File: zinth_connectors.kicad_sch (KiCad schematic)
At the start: 20 parts, among them J3 qwiic, J4 HeaderMale-2.54_1x16, J5 usb, J6 qwiic, J8 HeaderMale-2.54_1x16

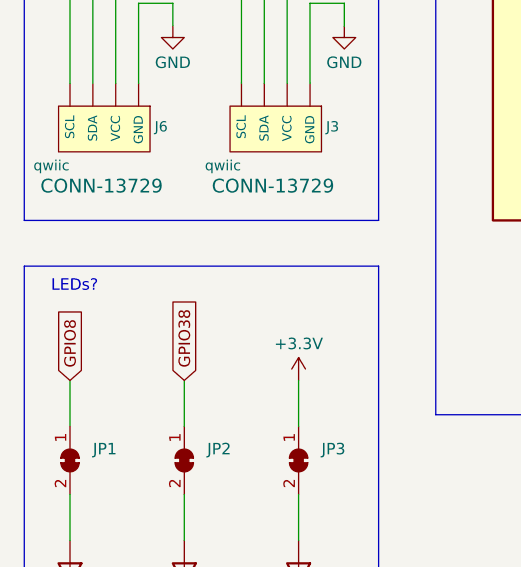
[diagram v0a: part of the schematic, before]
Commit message: added some stuff to schematic and PCB design
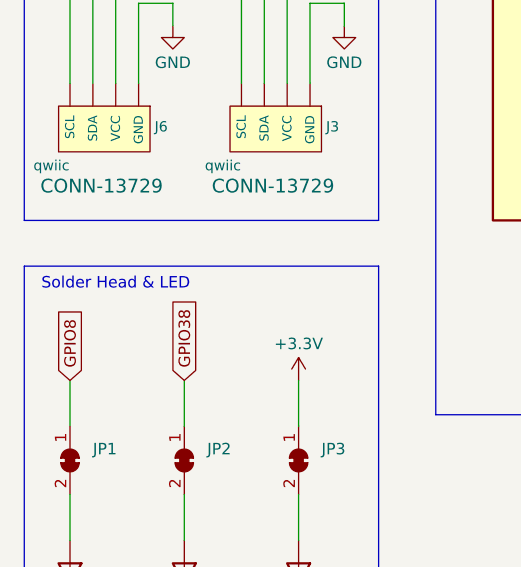
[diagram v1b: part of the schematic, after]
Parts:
- J4: footprint Conn_01x13_Pin -> Connector_PinHeader_2.54mm:PinHeader_1x16_P2.54mm_Vertical
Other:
- note added: "Solder Head & LED"
- note removed: "LEDs?"
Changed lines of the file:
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@@
 		)
 	)
-	(text "LEDs?"
+	(text "Solder Head & LED\n"
 		(exclude_from_sim no)
-		(at 42.418 91.186 0)
+		(at 46.99 90.932 0)
 		(effects
 			(font
@@
 			)
 		)
-		(property "Footprint" "Conn_01x13_Pin"
+		(property "Footprint" "Connector_PinHeader_2.54mm:PinHeader_1x16_P2.54mm_Vertical"
 			(at 199.39 55.88 0)
 			(hide yes)
